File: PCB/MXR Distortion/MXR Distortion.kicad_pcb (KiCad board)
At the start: 2 copper layers, 21 parts, among them J1 AudioJack2, J2 AudioJack2, J3 Barrel_Jack_MountingPin, U1 LM741

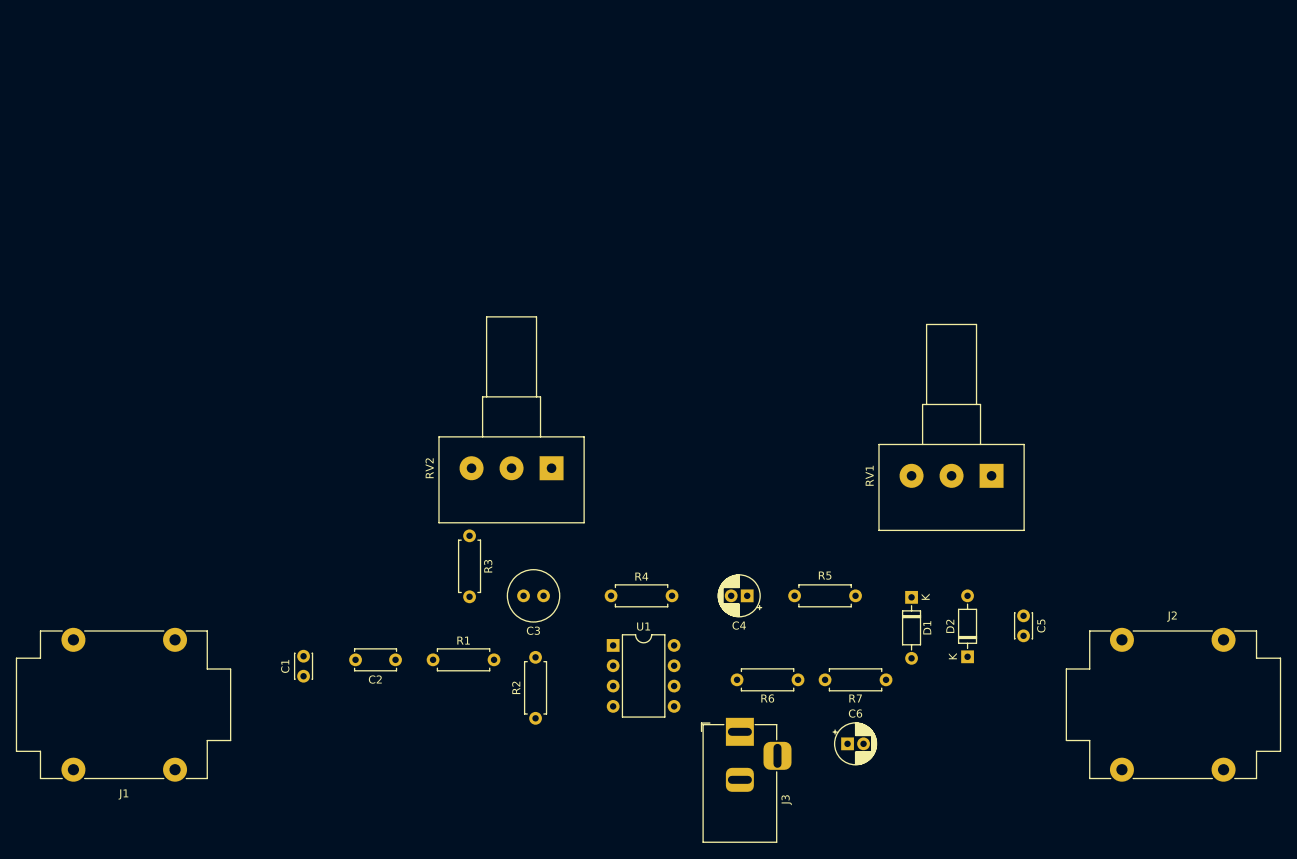
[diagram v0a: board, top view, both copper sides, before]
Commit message: PCB v1. Modify routes width
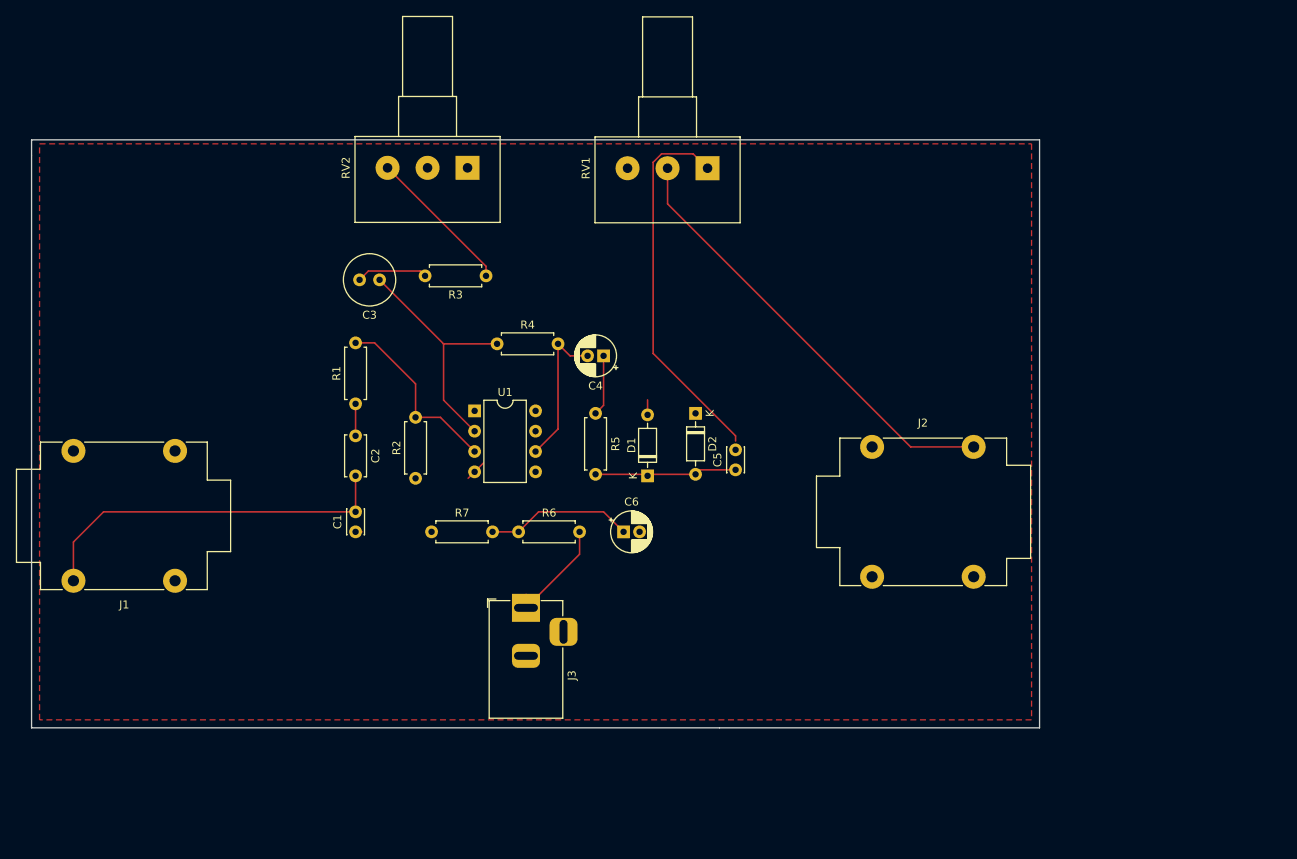
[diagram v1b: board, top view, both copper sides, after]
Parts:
- moved R7 59.7 mm to (119.0, 84.5), turned to 0 degrees
- moved RV1 52.3 mm to (153.5, 39.0)
- moved D2 45.6 mm to (152.0, 69.7), turned to -90 degrees
- moved C3 44.5 mm to (112.5, 53.0)
- moved C5 40.4 mm to (157.0, 76.8), turned to 90 degrees
- moved R6 39.5 mm to (129.9, 84.5), turned to 0 degrees
- moved J2 39.5 mm to (174.1, 73.9)
- moved RV2 39.0 mm to (123.5, 39.0)
- moved C6 38.6 mm to (143.0, 84.5)
- moved D1 36.3 mm to (146.0, 77.5), turned to 90 degrees
- moved C4 35.0 mm to (140.5, 62.5)
- moved R4 34.6 mm to (127.2, 61.0)
- moved U1 34.1 mm to (124.4, 69.4)
- moved R5 33.8 mm to (139.5, 69.7), turned to -90 degrees
- moved R2 33.5 mm to (117.0, 77.8)
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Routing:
- net Net-(D1-K): track 0.00 -> 65.0 mm
- net Net-(J2-PadS): track 0.00 -> 55.3 mm
- net Net-(C1-Pad2): track 0.00 -> 46.2 mm
- net Net-(U1--): track 0.00 -> 30.5 mm
- net Net-(U1-+): track 0.00 -> 23.1 mm
- net Net-(C4-Pad2): track 0.00 -> 18.9 mm
- net Net-(R3-Pad1): track 0.00 -> 18.6 mm
- net +4.5v: track 0.00 -> 18.5 mm
- net +9v: track 0.00 -> 14.0 mm
- net Net-(C3-Pad2): track 0.00 -> 8.89 mm
- net Net-(C4-Pad1): track 0.00 -> 7.60 mm
- net GND: track 0.00 -> 7.19 mm
- net Net-(C2-Pad1): track 0.00 -> 4.00 mm
- added copper zone on F.Cu, net GND
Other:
- board outline added: 126 x 73.5 mm

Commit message: PCB v1. Added ground plane
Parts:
- moved J1 10.1 mm to (96.5, 87.5)
- moved J2 7.43 mm to (167.1, 71.4)
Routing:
- net +9v: track 14.0 -> 45.5 mm
- net Net-(C1-Pad2): track 46.2 -> 32.5 mm
- net Net-(J2-PadS): track 55.3 -> 47.4 mm
- net Net-(D1-K): track 65.0 -> 71.5 mm
- net GND: track 7.19 -> 2.09 mm
- net Net-(C3-Pad2): track 8.89 -> 9.64 mm
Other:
- board size 126 x 73.5 mm -> 117 x 76 mm

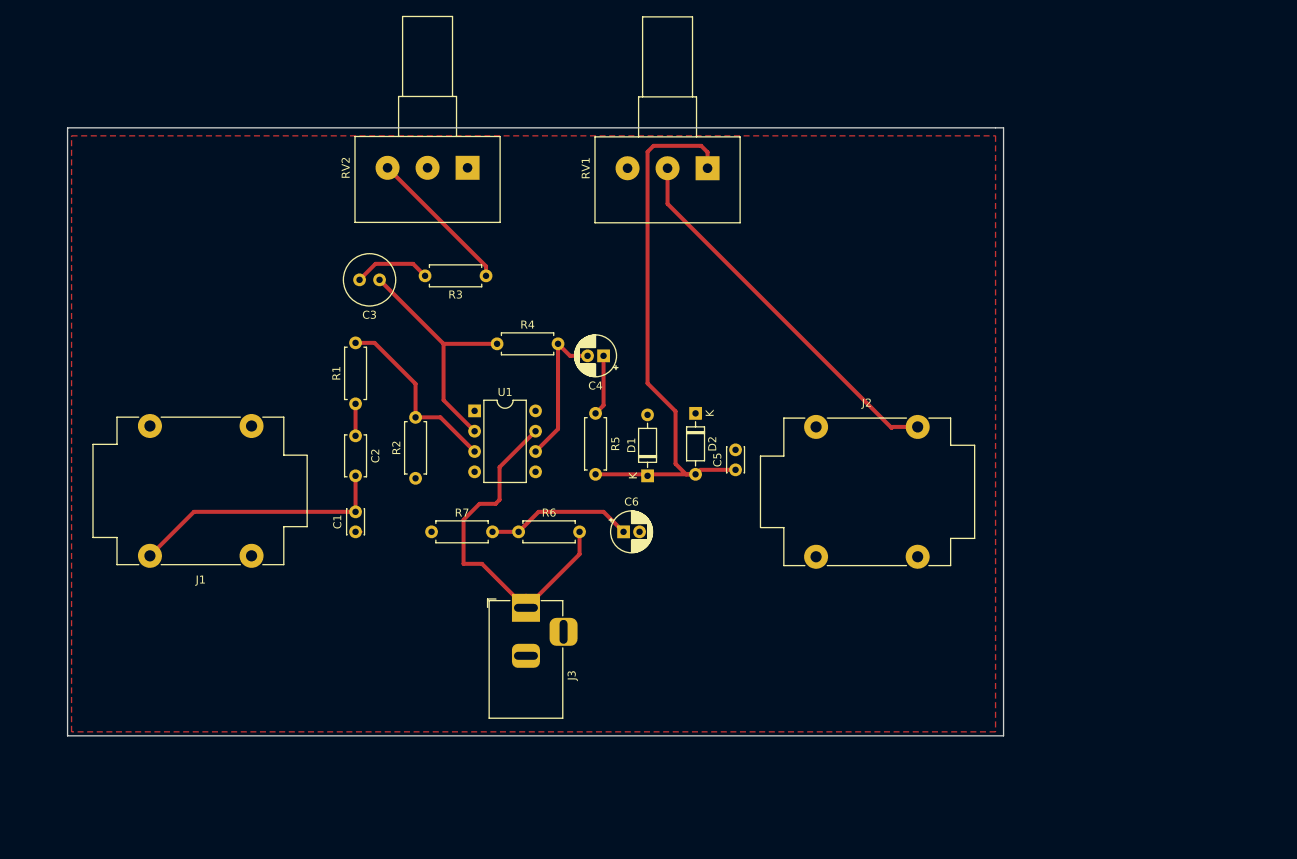
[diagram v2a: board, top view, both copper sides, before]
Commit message: Se cambio de lugar los potenciometros para reducir el tamano de la placa
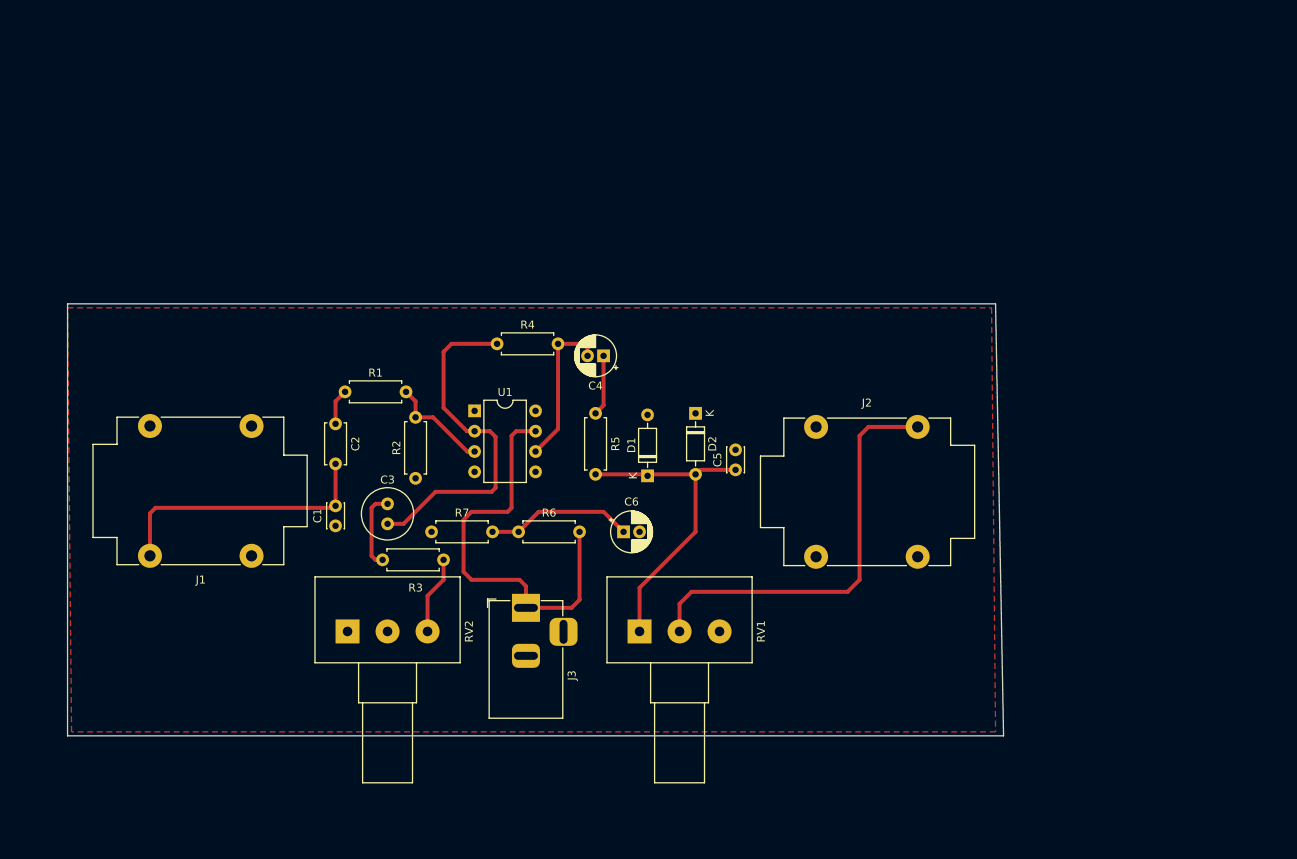
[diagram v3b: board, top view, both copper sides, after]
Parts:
- moved RV2 59.9 mm to (108.5, 97.0), turned to 90 degrees
- moved RV1 58.5 mm to (145.0, 97.0), turned to 90 degrees
- moved R3 35.9 mm to (120.5, 88.0)
- moved C3 30.5 mm to (113.5, 83.5), turned to 90 degrees
- moved C2 2.92 mm to (107.0, 71.0)
- moved C1 2.61 mm to (107.0, 83.8)
- moved R1 1.99 mm to (108.2, 67.0), turned to 0 degrees
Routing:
- net Net-(D1-K): track 71.5 -> 40.5 mm
- net Net-(U1--): track 30.5 -> 43.8 mm
- net Net-(U1-+): track 23.1 -> 12.8 mm
- net Net-(R3-Pad1): track 18.6 -> 8.52 mm
- net +9v: track 45.5 -> 53.9 mm
- net Net-(J2-PadS): track 47.4 -> 53.0 mm
- net Net-(C1-Pad2): track 32.5 -> 34.1 mm
- net GND: track 2.09 -> 0.71 mm
- net Net-(C4-Pad2): track 18.9 -> 19.5 mm
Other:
- board size 117 x 76 mm -> 117 x 54 mm
